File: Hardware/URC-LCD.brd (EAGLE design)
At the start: 48 x 29 mm, 6 parts, among them IC1 74HC2G125, J1 SPI-LCD

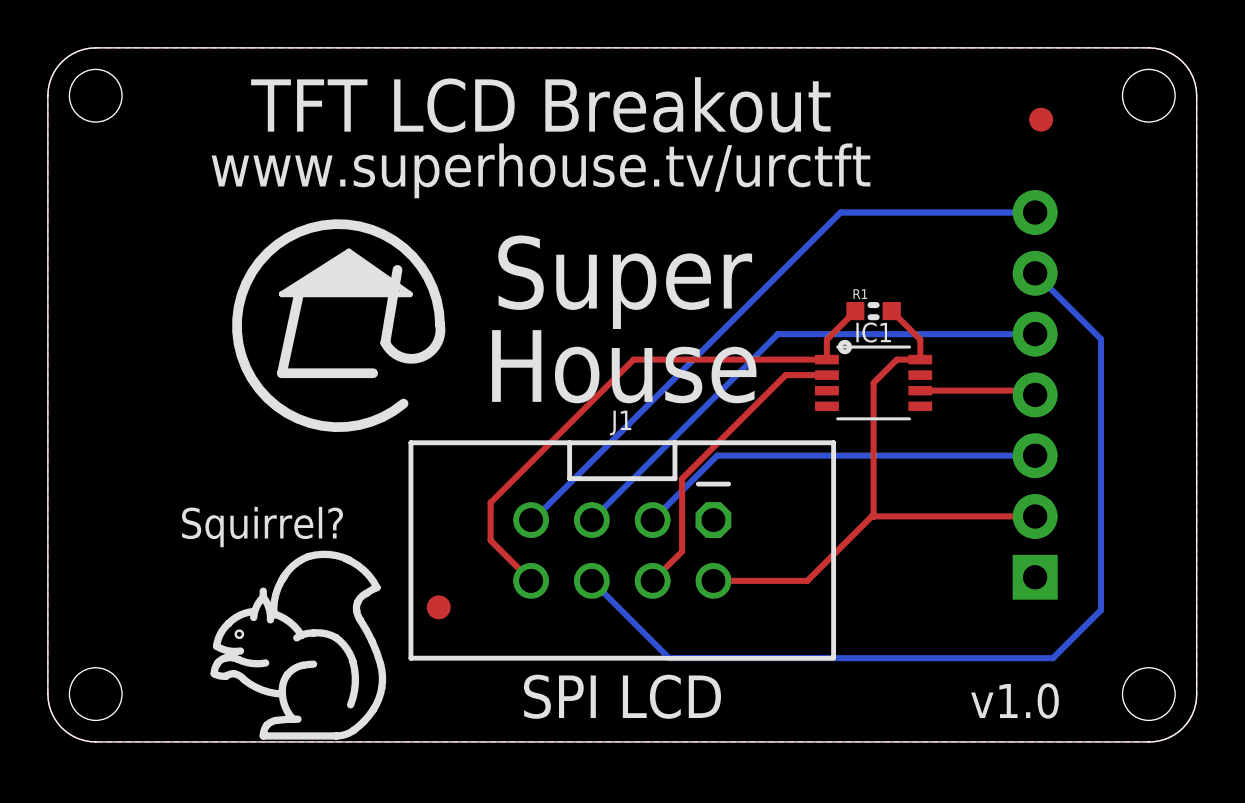
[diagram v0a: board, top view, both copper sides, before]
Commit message: Major mechanical shrinkage for revised v1.0 release.
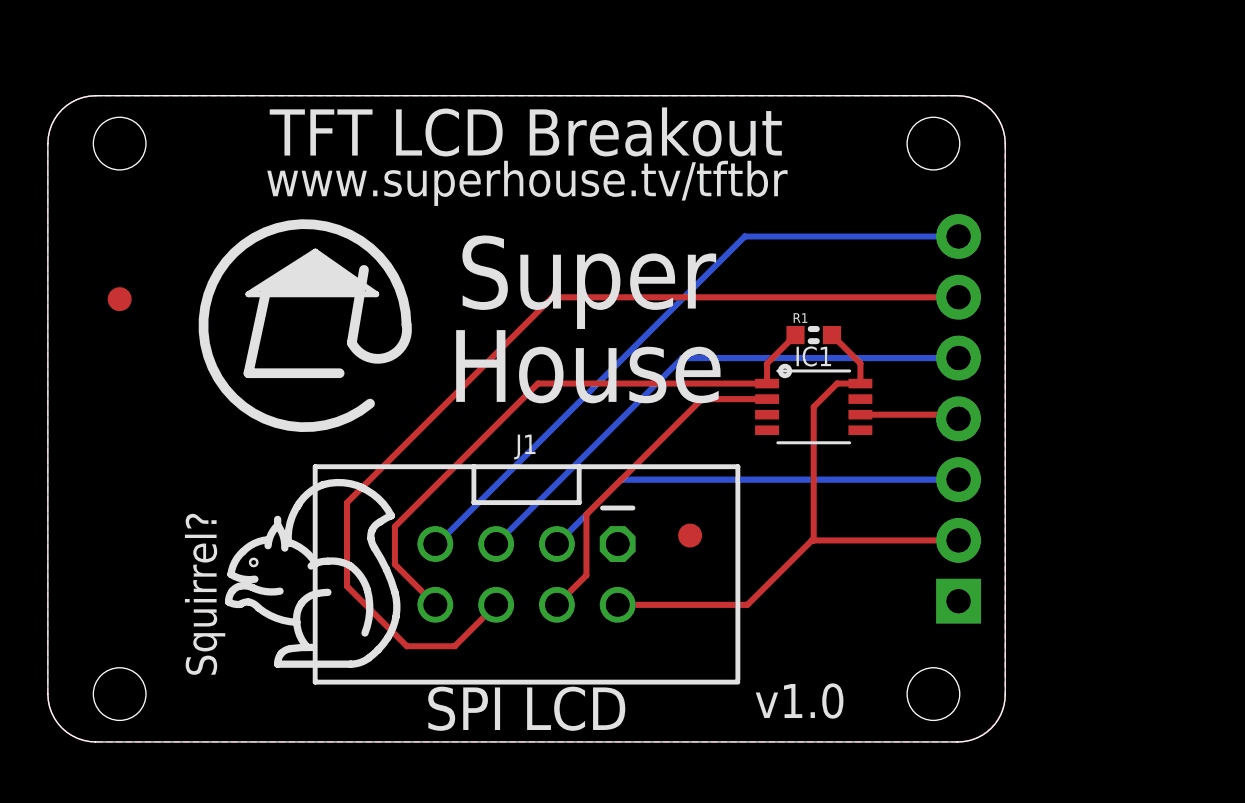
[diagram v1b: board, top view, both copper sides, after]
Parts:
- moved FID1 39.2 mm to (3.00, 18.5)
- moved FID3 10.9 mm to (26.8, 8.62)
- moved J1 4.12 mm to (20.0, 7.00)
- moved MOD1 3.35 mm to (23.3, 13.5)
- moved IC1 2.69 mm to (32.0, 14.0)
- moved R1 2.69 mm to (32.0, 17.0)
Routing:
- net TFT_DC: track 38.7 -> 40.6 mm
- net TFT_CS: track 23.0 -> 24.5 mm
- net COPI: track 12.6 -> 13.8 mm
- net TFT_RST: track 21.7 -> 22.5 mm
- net TFT_BLK: track 26.4 -> 27.2 mm
- net SCK: track 17.1 -> 17.9 mm
- net 3.3V: track 25.0 -> 25.8 mm
- net N$1: track 4.87 -> 4.13 mm
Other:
- board size 48 x 29 mm -> 40 x 27 mm
- board text added: "www.superhouse.tv/tftbr"
- board text removed: "www.superhouse.tv/urctft"

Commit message: Tie unused inputs to GND.
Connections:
- net GND: now also IC1.P$5, IC1.P$7
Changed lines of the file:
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@@
 <contactref element="IC1" pad="P$4"/>
 <contactref element="J1" pad="1"/>
+<contactref element="IC1" pad="P$5"/>
+<contactref element="IC1" pad="P$7"/>
 </signal>
 <signal name="3.3V">
